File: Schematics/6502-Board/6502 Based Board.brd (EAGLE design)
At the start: 114 x 88.9 mm, 19 parts, among them IC1 74HC14N, IC2 74HC74N, Q1 4MHz, U1 W65C02S-DIP

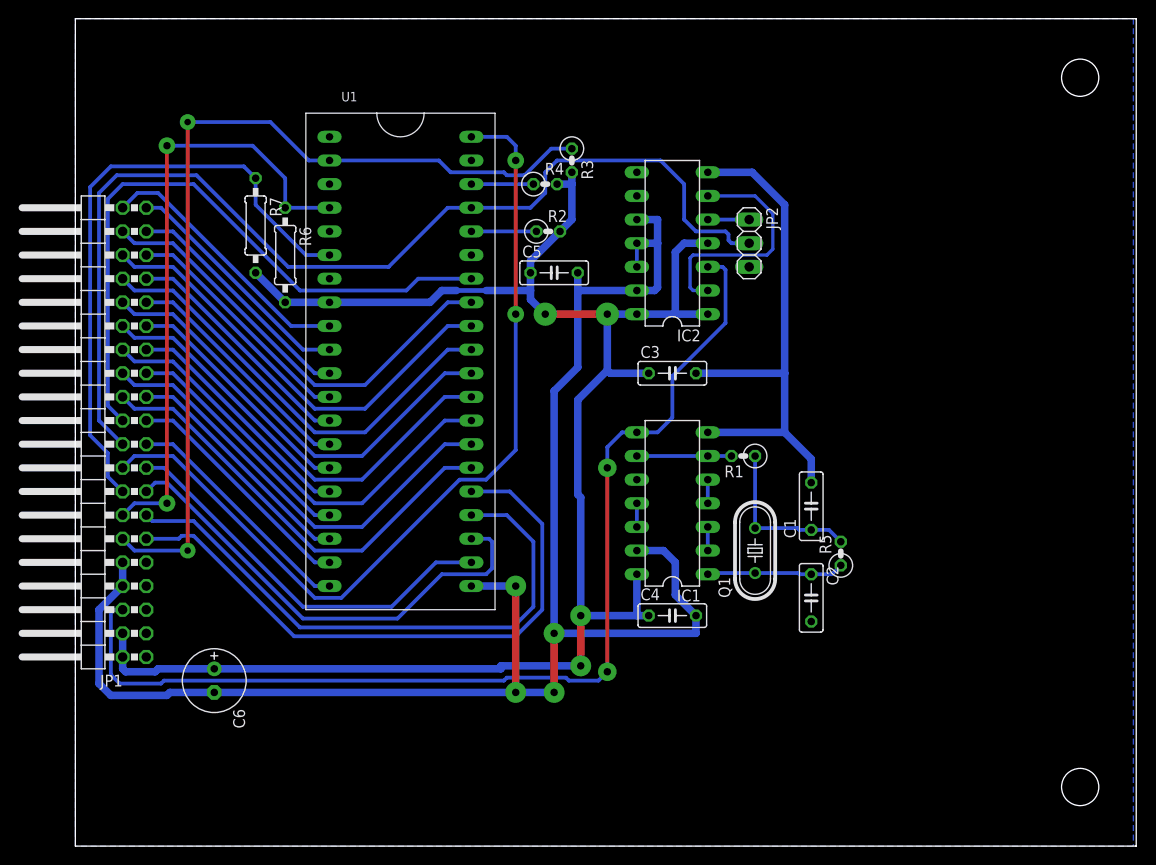
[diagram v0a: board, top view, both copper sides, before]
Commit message: Updated the processor board to add the following features:-
Added a header for NMI and IRQ status lights.

Reworked the circuit and added a header to allow 1, 2 and 4MHz clock speeds from the on-board oscillator.
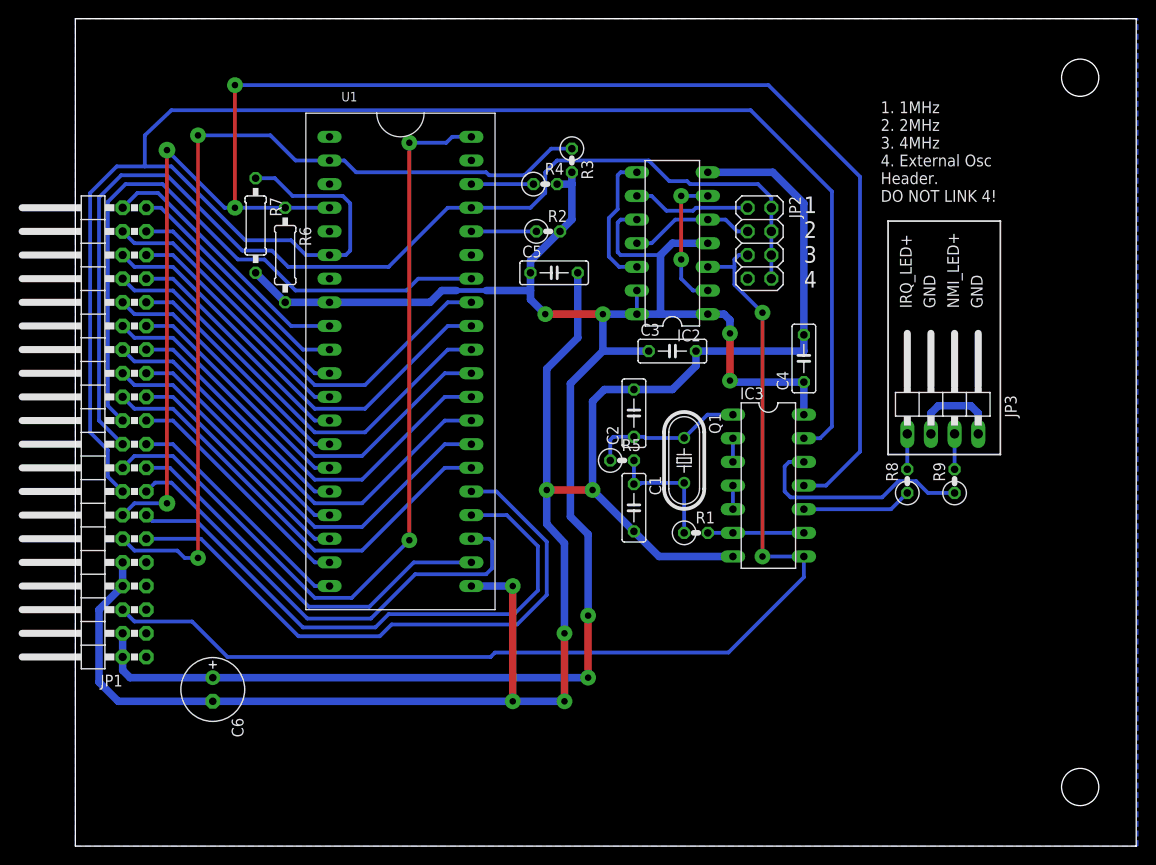
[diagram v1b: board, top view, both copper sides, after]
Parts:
- removed IC1: 74HC14N, 74xx-us:DIL14
- added IC3: 74HC04N, 74xx-eu:DIL14
- added JP3: (no value), pinhead:1X04/90
- added R8, R9: 1K, rcl:0207/2V
- JP2: device pinhead:1X03 -> pinhead:2X04
- moved C4 31.0 mm to (78.3, 52.4), turned to 90 degrees
- moved C2 27.5 mm to (60.0, 46.5), turned to 90 degrees
- moved R5 25.5 mm to (58.7, 41.4), turned to 0 degrees
- moved C1 19.1 mm to (60.0, 36.4), turned to 270 degrees
- moved Q1 12.3 mm to (65.4, 41.4), turned to 270 degrees
- moved R1 9.69 mm to (66.7, 33.7), turned to 0 degrees
- moved C3 2.38 mm to (64.1, 53.2)
- moved JP2 1.11 mm to (73.5, 64.8)
- moved C6 0.97 mm to (14.8, 16.8)
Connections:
- removed net N$6: IC1.11, IC1.12
- removed net PHI2_OUT: IC2.5, JP2.1
- new net 1MHZ: IC2.9, JP2.1
- new net 2MHZ: IC2.11, IC2.5, JP2.3
- new net IRQ_LED: JP3.1, R8.2
- new net N$11: IC3.10, R8.1
- new net N$12: IC3.12, R9.1
- new net N$8: IC2.12, IC2.8
- new net NMI_LED: JP3.3, R9.2
- net GND: now also IC3.7, JP2.7, JP3.2, JP3.4; no longer IC1.13, IC1.7, IC2.10, IC2.11, IC2.12, IC2.13, JP2.3
- net IRQB: now also IC3.11
- net N$2: now also IC3.4, IC3.5; no longer IC1.4, IC1.5
- net N$3: now also IC3.6, IC3.9; no longer IC1.6, IC1.9
- net N$5: now also IC3.1; no longer IC1.1
- net N$7: now also IC3.2, IC3.3; no longer IC1.2, IC1.3
- net NMIB: now also IC3.13
- net OSC: now also IC3.8, JP2.5; no longer IC1.8
- net PHI2: now also JP2.4, JP2.6, JP2.8
- net VCC: now also IC2.10, IC2.13, IC3.14; no longer IC1.14
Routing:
- net NMIB: track 66.4 -> 193.8 mm
- net IRQB: track 65.8 -> 184.7 mm, vias 2 -> 4
- net VCC: track 187.9 -> 214.2 mm, vias 4 -> 6
- net N$12: track 0.00 -> 24.7 mm
- net N$8: track 0.00 -> 14.8 mm
- net 2MHZ: track 0.00 -> 13.5 mm
- net 1MHZ: track 0.00 -> 12.7 mm
- net N$11: track 0.00 -> 11.8 mm
- net N$1: track 26.1 -> 15.1 mm, vias 0 -> 2
- net GND: track 235.9 -> 225.9 mm, vias 4 -> 6
- net OSC: track 115.3 -> 123.1 mm
- net PHI2: track 115.1 -> 121.3 mm
- net PHI2_OUT: track 4.45 -> 0.00 mm
- net N$4: track 17.6 -> 13.3 mm
- net NMI_LED: track 0.00 -> 3.81 mm
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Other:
- board text added: "1 2 3 4"
- board text added: "1. 1MHz 2. 2MHz 3. 4MHz 4. External Osc Header. DO NOT LINK 4!"
- board text added: "GND"
- board text added: "IRQ_LED+"
- board text added: "NMI_LED+"

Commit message: Updated to have a formal Timer IRQ.  Currently this is T1 on the W65C22 on the GPIO card, so if you want to use it that card must be present.
The prebuilt ROM ToEVID.bin uses this card at 0xC040.

A couple of minor whoopsies have been fixed as well.
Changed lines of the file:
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@@
 <?xml version="1.0" encoding="utf-8"?>
 <!DOCTYPE eagle SYSTEM "eagle.dtd">
-<eagle version="6.6.0">
+<eagle version="6.5.0">
 <drawing>
 <settings>
@@
 <element name="JP1" library="pinhead" package="2X20/90" value="" x="1.27" y="44.45" rot="R90"/>
 <element name="C5" library="rcl" package="C050-025X075" value="100nF" x="51.435" y="61.595"/>
-<element name="R2" library="rcl" package="0207/2V" value="1K" x="50.8" y="66.04"/>
-<element name="R3" library="rcl" package="0207/2V" value="10K" x="53.34" y="73.66" rot="R270"/>
-<element name="R4" library="rcl" package="0207/2V" value="10K" x="50.4825" y="71.12"/>
+<element name="R2" library="rcl" package="0207/2V" value="1K" x="50.8" y="66.04" smashed="yes">
+<attribute name="NAME" x="47.5742" y="67.691" size="1.27" layer="25" ratio="10"/>
+<attribute name="VALUE" x="50.4317" y="67.6148" size="1.27" layer="27" ratio="10"/>
+</element>
+<element name="R3" library="rcl" package="0207/2V" value="10K" x="53.34" y="73.66" smashed="yes" rot="R270">
+<attribute name="NAME" x="54.8767" y="76.10475" size="1.27" layer="25" ratio="10"/>
+<attribute name="VALUE" x="54.8767" y="74.2823" size="1.27" layer="27" ratio="10"/>
+</element>
+<element name="R4" library="rcl" package="0207/2V" value="10K" x="50.4825" y="71.12" smashed="yes">
+<attribute name="NAME" x="47.2567" y="74.676" size="1.27" layer="25" ratio="10"/>
+<attribute name="VALUE" x="47.2567" y="72.85355" size="1.27" layer="27" ratio="10"/>
+</element>
 <element name="C6" library="rcl" package="E2,5-7" value="47uF" x="14.76375" y="16.8275" rot="R270"/>
 <element name="R5" library="rcl" package="0207/2V" value="1M" x="58.7375" y="41.43375"/>
